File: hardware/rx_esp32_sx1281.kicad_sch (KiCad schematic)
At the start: 24 parts, among them SW1 SKUBAAE010, U16 ESP32-PICO-V3, U18 SX1281, X3 52MHz TCXO

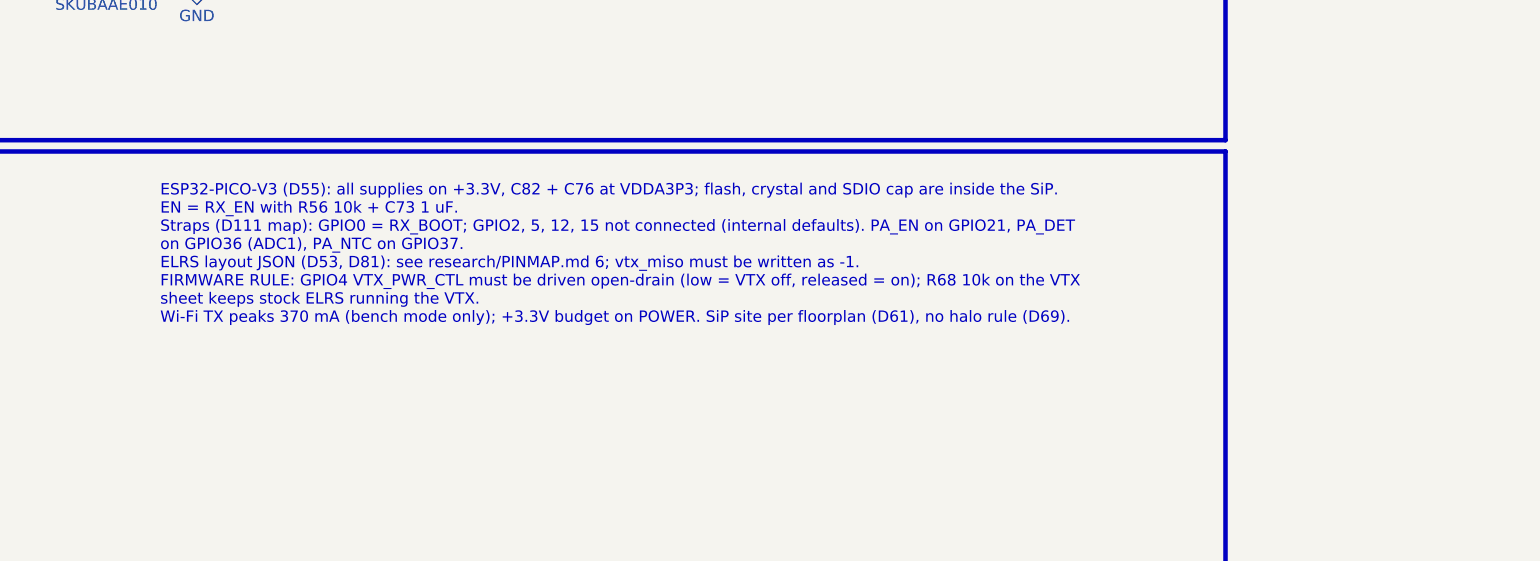
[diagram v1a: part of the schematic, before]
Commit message: 5 V input: two Schottky diodes replace the TPS2116 mux and the SGM40661 (D118)
D9 VBUS -> +5V and D10 +5V_BST -> +5V, MSKSEMI MS2A40LDF DFN1610-2
(LCSC C7380000, imported with import_part.py; land spec PASS). U3, R7,
R8, U24, C131 removed; C128 is +5V bulk; PWR_FLAG on +5V. Board synced.

Stale schematic notes rewritten (O4 switch block now "HD_EN PULL-DOWN",
TVS, INA186 input RC, PA NTC, R67, GPIO4 control, root power table).

ERC 0 errors; check_netlist 7 ok; sch_integrate --check clean;
setup_board --check up to date; board_spec 31/31; sync dry run 0 changes;
DRC unchanged.

Co-Authored-By: Claude Opus 5.5 <noreply@anthropic.com>
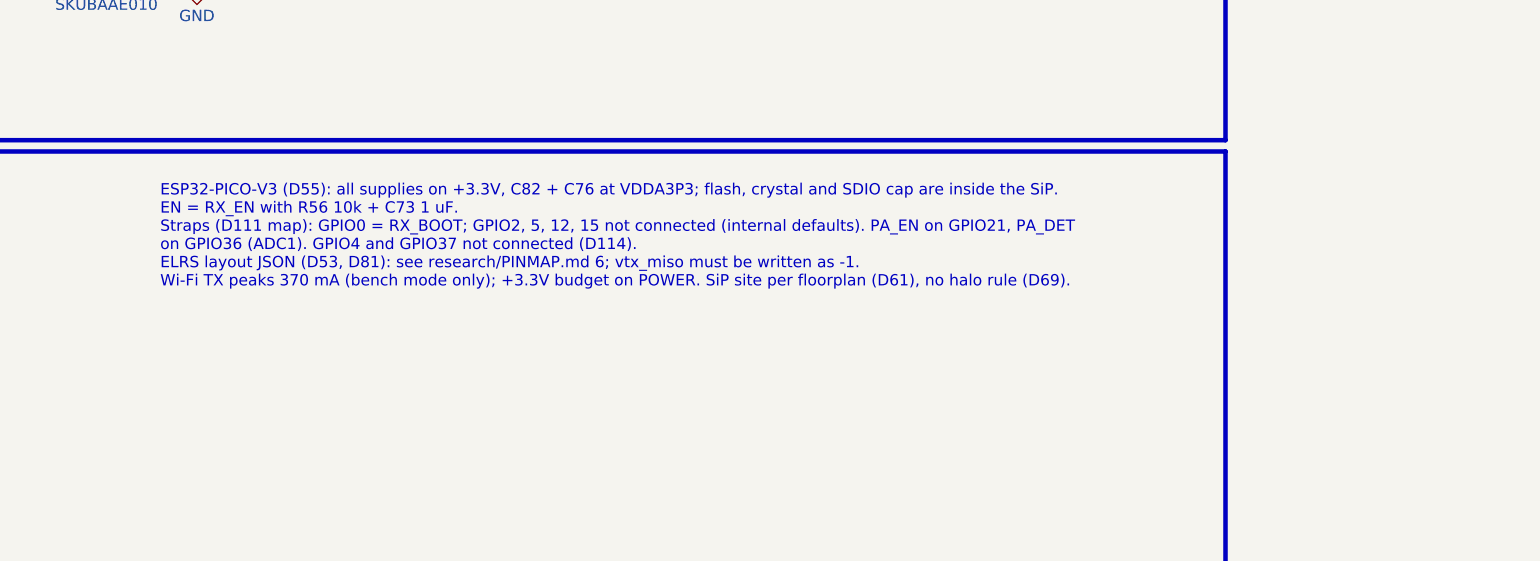
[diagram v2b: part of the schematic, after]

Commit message: Footprint audit vs datasheets, 0201 lands to Murata minimum, schematic notes shortened
Footprints: 45 checked against their datasheets by group, no pin or
land errors. C/R/L_0201_..._L pad height 0.28 -> 0.30 (Murata GRM03
reflow table c >= 0.30); other lands already at least density per D109
and left unchanged. Land spec texts cleaned (sources, shared parts).

Schematic notes: 157 -> 152 items, 19.5k -> 9.7k characters, all
current (diode-OR, removed parts, RTC6705 filters, TX0/RX0).

check_footprint 107/107 lib specs PASS; ERC 0 errors / 2 warnings;
check_netlist 7 ok; sch_integrate --check clean. Board not synced.

Co-Authored-By: Claude Opus 5.5 <noreply@anthropic.com>
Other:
- note added: "BOOT / BIND BUTTON"
- note added: "WI-FI CHIP ANTENNA"
- note removed: "BOOT / BIND BUTTON (D65)"
- note removed: "Wi-Fi CHIP ANTENNA (D58)"
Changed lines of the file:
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@@
 		)
 	)
-	(text "Wi-Fi CHIP ANTENNA (D58)"
+	(text "WI-FI CHIP ANTENNA"
 		(exclude_from_sim no)
 		(at 148.59 181.61 0)
@@
 		)
 	)
-	(text "BOOT / BIND BUTTON (D65)"
+	(text "BOOT / BIND BUTTON"
 		(exclude_from_sim no)
 		(at 207.01 49.53 0)
@@
 		)
 	)
-	(text_box "RFIO -> FL1 2450FM07D0034T filter (DC-blocked) -> RF_RX_ANT 50 Ohm -> AE1 lambda/4 wire (about 28-29 mm, trimmed in V7), DNP. RF class."
+	(text_box "RFIO -> FL1 filter (DC-blocked) -> 50 Ohm RF_RX_ANT -> AE1 lambda/4 wire (about 28-29 mm), DNP. RF class."
 		(exclude_from_sim no)
 		(at 172.72 127 0)
@@
 		)
 	)
-	(text_box "Shared boot / bind button (D65): SW1 to GND, D8 dual Schottky to FC_BOOT (RP2354A QSPI_SS via R44) and RX_BOOT (ESP32 GPIO0). Released, the diodes isolate the two straps.\nHeld at power-up: RP2354A BOOTSEL + ESP32 download mode (recovery, D67). Pressed while running: ELRS bind / Wi-Fi / reboot, the FC keeps running."
+	(text_box "SW1 to GND, D8 dual Schottky to FC_BOOT and RX_BOOT: released, the diodes isolate the two straps.\nHeld at power-up: RP2354A BOOTSEL + ESP32 download. Pressed while running: ELRS bind / Wi-Fi."
 		(exclude_from_sim no)
 		(at 294.64 50.8 0)
@@
 		)
 	)
-	(text_box "ESP32-PICO-V3 (D55): all supplies on +3.3V, C82 + C76 at VDDA3P3; flash, crystal and SDIO cap are inside the SiP. EN = RX_EN with R56 10k + C73 1 uF.\nStraps (D111 map): GPIO0 = RX_BOOT; GPIO2, 5, 12, 15 not connected (internal defaults). PA_EN on GPIO21, PA_DET on GPIO36 (ADC1). GPIO4 and GPIO37 not connected (D114).\nELRS layout JSON (D53, D81): see research/PINMAP.md 6; vtx_miso must be written as -1.\nWi-Fi TX peaks 370 mA (bench mode only); +3.3V budget on POWER. SiP site per floorplan (D61), no halo rule (D69)."
+	(text_box "ESP32-PICO-V3: supplies on +3.3V, C82 + C76 at VDDA3P3; flash and crystal are in the SiP. EN = RX_EN with R56 10k + C73 1 uF.\nGPIO0 = RX_BOOT, PA_EN GPIO21, PA_DET GPIO36. Wi-Fi TX peaks 370 mA."
 		(exclude_from_sim no)
 		(at 284.48 100.33 0)
@@
 		)
 	)
-	(text_box "SX1281 from OpenRX-Lite-UFL (D52, D53): LDO mode (DCC_SW open, no inductor), VREG_RADIO with C87 + C88, decoupling per DS Table 15-1. Pin 5 is GND and is grounded here. 52 MHz TCXO X3 AC-coupled by C84 into XTA."
+	(text_box "SX1281: LDO mode (DCC_SW open, no inductor), VREG_RADIO C87 + C88. Pin 5 is GND. 52 MHz TCXO X3 AC-coupled by C84 into XTA."
 		(exclude_from_sim no)
 		(at 38.1 139.7 0)
@@
 		)
 	)
-	(text_box "Wi-Fi (D58): LNA_IN -> RF_WIFI 50 Ohm (<= 8 mm, D69) -> pi match C133 (DNP) / R88 0R / C132 (DNP) -> AE2 chip antenna; values from V7 tuning. Keep-out per DRU (D21)."
+	(text_box "LNA_IN -> RF_WIFI 50 Ohm (<= 8 mm) -> pi match C133 (DNP) / R88 0R / C132 (DNP) -> AE2 chip antenna. Keep-out per DRU."
 		(exclude_from_sim no)
 		(at 152.4 208.28 0)
@@
 		)
 	)
-	(text_box "D4 RGB LED (ELRS led_rgb GPIO32) from OpenRX-Lite-UFL. P4-15 DECIDED: keep on +3.3V as the house RX boards do (0.2 V under the datasheet VDD minimum; on +5V the DIN level would be short). Bench V-LED; fallback VDD to +5V."
+	(text_box "D4 RGB LED (GPIO32) on +3.3V, 0.2 V under the datasheet VDD minimum: bench-check; fallback VDD to +5V."
 		(exclude_from_sim no)
 		(at 38.1 215.9 0)
@@
 		(margins 0.9525 0.9525 0.9525 0.9525)
 		(stroke
-			(width -0.0001)
-			(type solid)
-		)
-		(fill
-			(type none)
-		)
-		(effects
-			(font
-				(size 1.27 1.27)
-			)
-			(justify left top)
-		)
-	)
-	(text_box "RX sheet: radio, TCXO, RGB LED and Wi-Fi match copied from OpenRX-Lite-UFL (D52, D53, D58); ESP32-PICO-V3 block new from Espressif Fig. 11 (D55); shared boot / bind button new (D65). Pin plan research/PINMAP.md 6, parts hardware/bom_plan.json, +3.3V from POWER."
-		(exclude_from_sim no)
-		(at 205.74 27.94 0)
-		(size 198.12 7.62)
-		(margins 0.9525 0.9525 0.9525 0.9525)
-		(stroke
